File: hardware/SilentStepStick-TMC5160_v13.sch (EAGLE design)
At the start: 39 parts, among them IC1 TMC5160-WA, IC2 FDMC8030, IC3 FDMC8030, IC4 FDMC8030, IC5 FDMC8030, P1 MA08-1, P2 MA08-1, P3 MA02-1, X1 PASSER-04, X2 PASSER-04, X3 PASSER-04, X4 PASSER-04

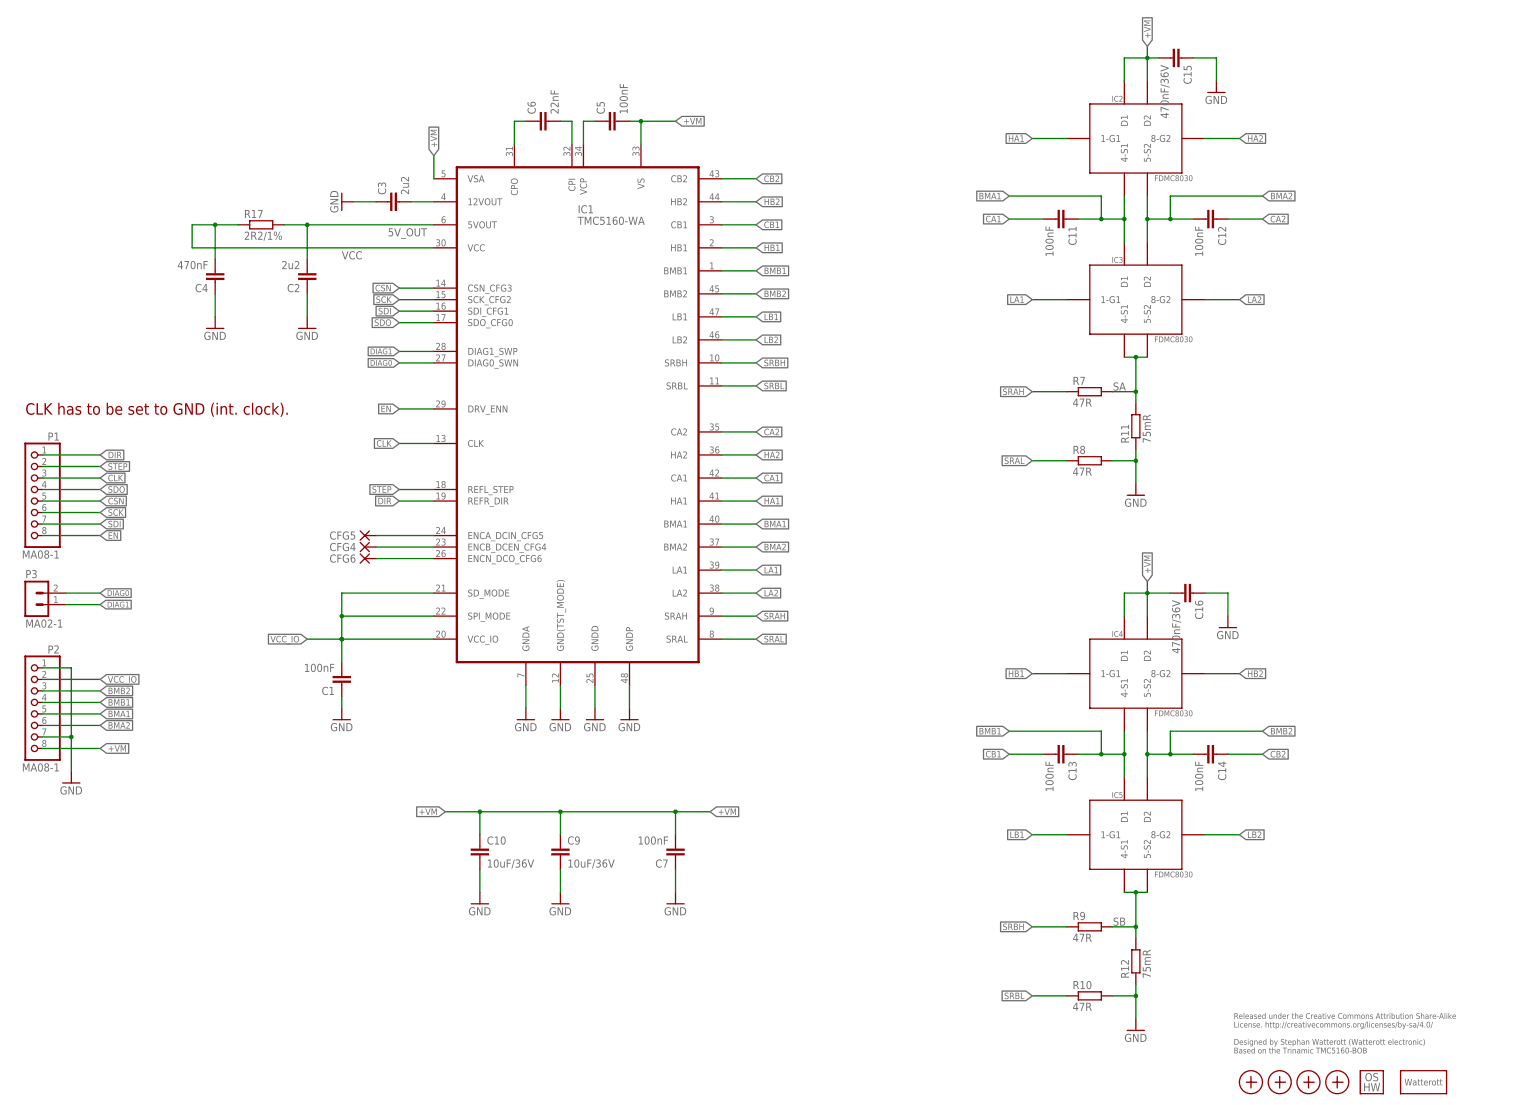
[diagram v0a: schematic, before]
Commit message: updated schematics
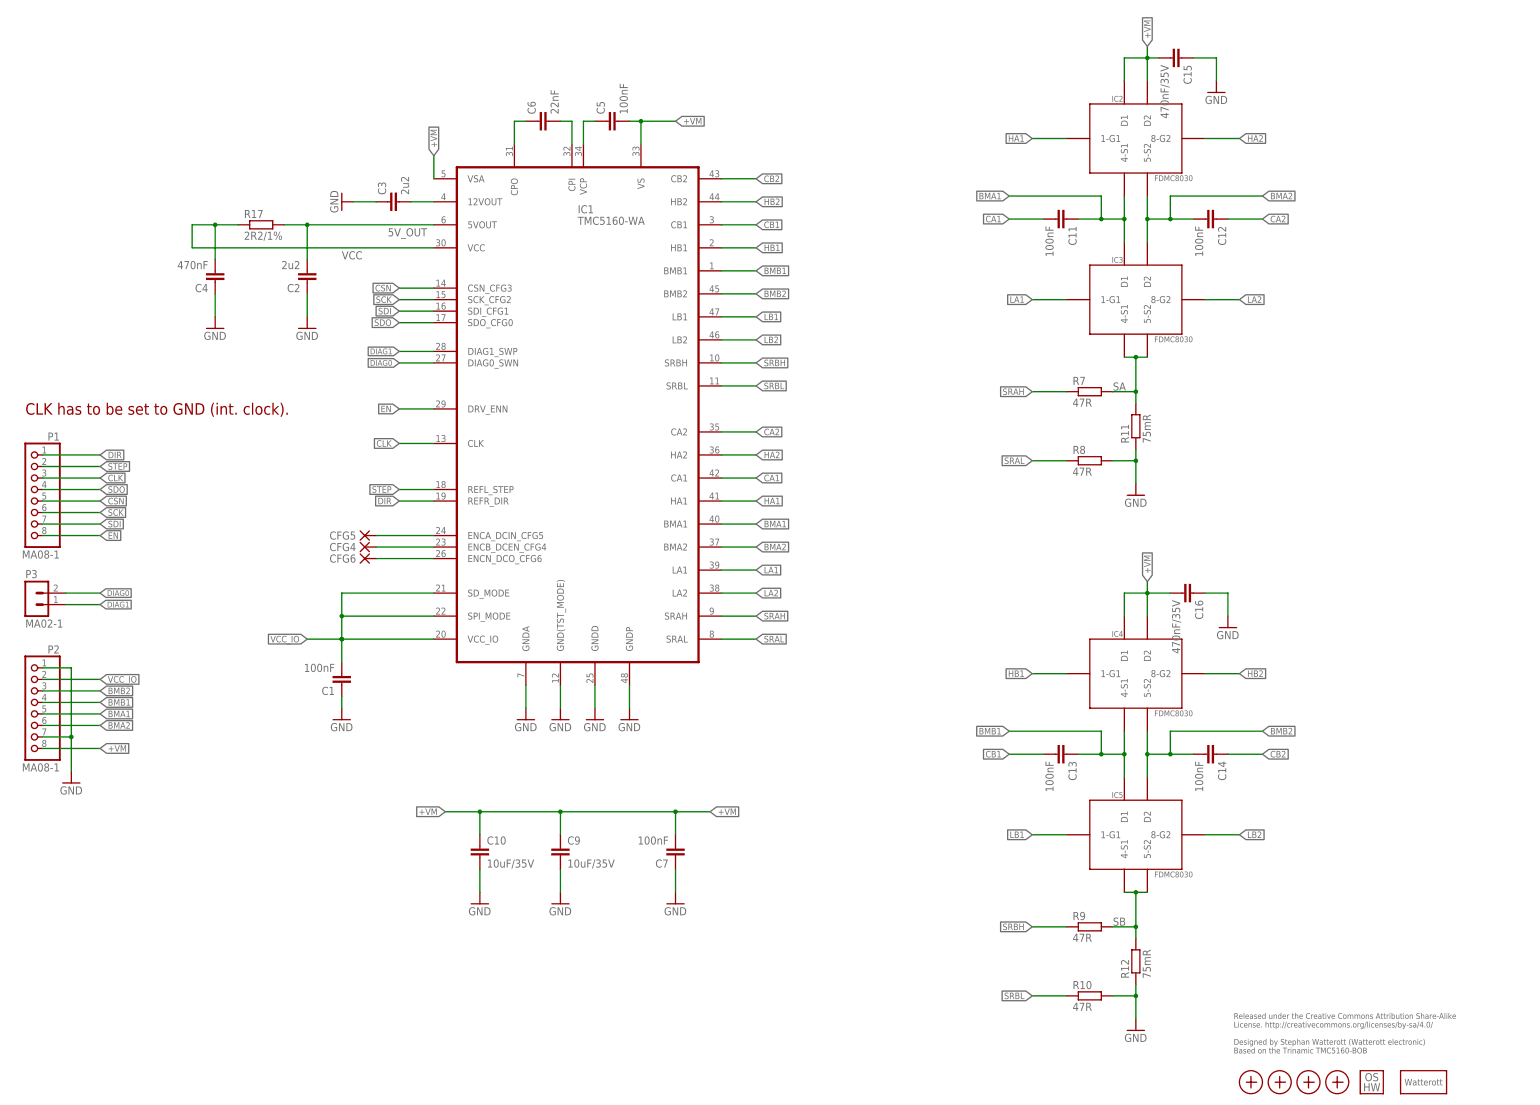
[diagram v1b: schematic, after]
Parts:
- C10, C9: value 10uF/36V -> 10uF/35V
- C15, C16: value 470nF/36V -> 470nF/35V
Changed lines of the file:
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@@
 <part name="GND11" library="supply1" deviceset="GND" device=""/>
 <part name="C7" library="rcl" deviceset="C-EU" device="C0402" value="100nF"/>
-<part name="C9" library="rcl" deviceset="C-EU" device="C0805" value="10uF/36V"/>
-<part name="C10" library="rcl" deviceset="C-EU" device="C0805" value="10uF/36V"/>
+<part name="C9" library="rcl" deviceset="C-EU" device="C0805" value="10uF/35V"/>
+<part name="C10" library="rcl" deviceset="C-EU" device="C0805" value="10uF/35V"/>
 <part name="GND14" library="supply1" deviceset="GND" device=""/>
 <part name="GND15" library="supply1" deviceset="GND" device=""/>
 <part name="GND18" library="supply1" deviceset="GND" device=""/>
-<part name="C15" library="rcl" deviceset="C-EU" device="C0402" value="470nF/36V"/>
+<part name="C15" library="rcl" deviceset="C-EU" device="C0402" value="470nF/35V"/>
 <part name="GND16" library="supply1" deviceset="GND" device=""/>
 <part name="IC2" library="Fairchild_By_element14_Batch_1" deviceset="FDMC8030" device="" value="FDMC8030"/>
@@
 <part name="IC4" library="Fairchild_By_element14_Batch_1" deviceset="FDMC8030" device="" value="FDMC8030"/>
 <part name="IC5" library="Fairchild_By_element14_Batch_1" deviceset="FDMC8030" device="" value="FDMC8030"/>
-<part name="C16" library="rcl" deviceset="C-EU" device="C0402" value="470nF/36V"/>
+<part name="C16" library="rcl" deviceset="C-EU" device="C0402" value="470nF/35V"/>
 <part name="GND20" library="supply1" deviceset="GND" device=""/>
 <part name="C13" library="rcl" deviceset="C-EU" device="C0402" value="100nF"/>
